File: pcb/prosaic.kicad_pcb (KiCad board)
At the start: 2 copper layers, 347.9 x 95.4 mm, 162 parts, among them J1 USB_C_Receptacle, K1 ESC, K10 WIN, K11 2, K12 W, K13 S, K14 X, K15 LALT, K16 3, K17 E, K18 D, K19 C, K2 TAB, K20 SPACE, K21 4, K22 R, K23 F, K24 V, K25 RALT, K26 5, K27 T, K28 G, K29 B, K3 CAPSLK, K30 FN, K31 6, K32 Y, K33 H, K34 N, K35 MENU, K36 7, K37 U, K38 J, K39 M, K4 LSHIFT, K40 RCTRL, K41 8, K42 I, K43 K, K44 ,, K45 LEFT, K46 9, K47 O, K48 L, K49 ., K5 LCTRL, K50 DOWN, K51 0, K52 P, K53 ;, K54 /, K55 RIGHT, K56 -, K57 [, K58 ', K59 RSHIFT, K6 1, K60 =, K61 ], K62 ENTER, K63 UP, K64 BCKSPC, K65 \, K66 HOME, K67 END, K68 INS, K69 DEL, K7 Q, K70 PGUP, K71 PGDWN, K8 A, K9 Z, SW1 SW_PUSH, U1 ATMEGA32U4, X1 XTAL_GND

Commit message: Made moutning hole rearrangements
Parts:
- removed the REF** at (50.3, 118.8)
- removed the REF** at (388.1, 118.8)
- removed the REF** at (281.7, 137.5)
- removed the REF** at (193.0, 109.2)
- added REF**: MountingHole_3.2mm_M3_ISO7380_Pad, MountingHole:MountingHole_3.2mm_M3_ISO7380_Pad, F.Cu at (388.1, 118.1)
- added REF**: MountingHole_3.2mm_M3_ISO7380_Pad, MountingHole:MountingHole_3.2mm_M3_ISO7380_Pad, F.Cu at (278.7, 146.3)
- added REF**: MountingHole_3.2mm_M3_ISO7380_Pad, MountingHole:MountingHole_3.2mm_M3_ISO7380_Pad, F.Cu at (245.4, 89.8)
- added REF**: MountingHole_3.2mm_M3_ISO7380_Pad, MountingHole:MountingHole_3.2mm_M3_ISO7380_Pad, F.Cu at (164.4, 146.3)
- added REF**: MountingHole_3.2mm_M3_ISO7380_Pad, MountingHole:MountingHole_3.2mm_M3_ISO7380_Pad, F.Cu at (131.1, 89.8)
- added REF**: MountingHole_3.2mm_M3_ISO7380_Pad, MountingHole:MountingHole_3.2mm_M3_ISO7380_Pad, F.Cu at (50.3, 118.1)
- turned R3 to 180 degrees
- turned R4 to 180 degrees
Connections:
- D66 pad 1: /row2 -> /row0
- D67 pad 1: /row3 -> /row1
- D70 pad 1: /row2 -> /row0
- D71 pad 1: /row3 -> /row1
- K20 pad 1: /col3 -> /col5
- K25 pad 1: /col4 -> /col9
- K30 pad 1: /col5 -> /col10
- K35 pad 1: /col6 -> /col11
- K40 pad 1: /col7 -> /col12
- K45 pad 1: /col8 -> /col14
- K50 pad 1: /col9 -> /col15
- K55 pad 1: /col10 -> /col16
- K63 pad 1: /col12 -> /col15
- K66 pad 1: /col13 -> /col15
- K67 pad 1: /col13 -> /col15
- K70 pad 1: /col14 -> /col16
- K71 pad 1: /col14 -> /col16
- U1 pad 36: Net-(U1-Pad36) -> /col16
- U1 pad 37: Net-(U1-Pad37) -> /col15
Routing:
- net /col4: track 426.6 -> 0.00 mm, vias 1 -> 0
- net /row3: track 413.5 -> 0.00 mm, vias 4 -> 0
- net /col0: track 405.1 -> 0.00 mm, vias 1 -> 0
- net /row2: track 395.3 -> 0.00 mm, vias 4 -> 0
- net /col1: track 393.5 -> 0.00 mm, vias 4 -> 0
- net /row4: track 373.7 -> 0.00 mm, vias 1 -> 0
- net /row0: track 361.9 -> 0.00 mm, vias 7 -> 0
- net /row1: track 334.1 -> 0.00 mm, vias 3 -> 0
- net /col3: track 323.9 -> 0.00 mm, vias 4 -> 0
- net /col5: track 271.1 -> 0.00 mm, vias 3 -> 0
- net /col6: track 257.3 -> 0.00 mm, vias 1 -> 0
- net /col7: track 240.2 -> 0.00 mm, vias 1 -> 0
- net /col10: track 238.0 -> 0.00 mm
- net /col8: track 224.9 -> 0.00 mm, vias 1 -> 0
- net /col9: track 224.8 -> 0.00 mm, vias 1 -> 0
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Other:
- board size 347.9 x 95.4 mm -> 347.9 x 95.5 mm

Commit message: WIP: Ready for stabilizer verification
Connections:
- K11 pad 1: Net-(K11-Pad1) -> /col2
- K12 pad 1: Net-(K11-Pad1) -> /col2
- K13 pad 1: Net-(K11-Pad1) -> /col2
- K14 pad 1: Net-(K11-Pad1) -> /col2
- K15 pad 1: Net-(K11-Pad1) -> /col2
- U1 pad 10: /row2 -> /col0
- U1 pad 11: /row3 -> /col1
- U1 pad 12: /col2 -> /row2
- U1 pad 18: /col3 -> /col14
- U1 pad 19: /col4 -> /col15
- U1 pad 20: /col5 -> /col16
- U1 pad 21: /col6 -> /row0
- U1 pad 22: /col8 -> /row1
- U1 pad 25: /col7 -> /row4
- U1 pad 26: /col9 -> /row3
- U1 pad 27: /col10 -> /col13
- U1 pad 28: /row4 -> /col12
- U1 pad 29: /col0 -> /col11
- U1 pad 30: /col1 -> /col10
- U1 pad 31: Net-(U1-Pad31) -> /col9
- U1 pad 32: Net-(U1-Pad32) -> /col8
- U1 pad 36: /col16 -> /col7
- U1 pad 37: /col15 -> /col6
- U1 pad 38: /col14 -> /col5
- U1 pad 39: /col13 -> /col4
- U1 pad 40: /col12 -> /col3
- U1 pad 41: /col11 -> /col2
- U1 pad 8: /row0 -> Net-(U1-Pad8)
- U1 pad 9: /row1 -> Net-(U1-Pad9)

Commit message: Completed revision with new PCB layout
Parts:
- K20: footprint keebs:Mx_Alps_625 -> keebs:Mx_Alps_625_reverse
- moved SW1 0.64 mm to (327.8, 120.4)
- moved J1 0.44 mm to (332.9, 74.6)
- moved R1 0.15 mm to (327.8, 114.2)
- moved C4 0.11 mm to (352.7, 123.9)
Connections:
- D55 pad 1: /row4 -> /row3
- K45 pad 1: /col14 -> /col16
- U1 pad 11: /col1 -> /row2
- U1 pad 12: /row2 -> /col13
- U1 pad 27: /col13 -> /col12
- U1 pad 28: /col12 -> /col11
- U1 pad 29: /col11 -> /col2
- U1 pad 30: /col10 -> /col3
- U1 pad 31: /col9 -> /col4
- U1 pad 32: /col8 -> /col5
- U1 pad 36: /col7 -> /col6
- U1 pad 37: /col6 -> /col7
- U1 pad 38: /col5 -> /col8
- U1 pad 39: /col4 -> /col9
- U1 pad 40: /col3 -> /col10
- U1 pad 41: /col2 -> Net-(U1-Pad41)
- U1 pad 9: Net-(U1-Pad9) -> /col1
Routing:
- net /row0: track 0.00 -> 417.9 mm, vias 0 -> 1
- net /col0: track 0.00 -> 408.4 mm, vias 0 -> 2
- net /col2: track 0.00 -> 405.8 mm
- net /col1: track 0.00 -> 396.4 mm, vias 0 -> 2
- net /col3: track 0.00 -> 360.4 mm
- net /row4: track 0.00 -> 359.8 mm
- net /row3: track 0.00 -> 359.6 mm, vias 0 -> 1
- net /row1: track 0.00 -> 357.3 mm, vias 0 -> 1
- net /col4: track 0.00 -> 341.2 mm
- net /col5: track 0.00 -> 321.5 mm
- net /col6: track 0.00 -> 302.8 mm
- net /row2: track 0.00 -> 292.2 mm, vias 0 -> 1
- net /col7: track 0.00 -> 282.9 mm
- net /col8: track 0.00 -> 260.0 mm
- net /col9: track 0.00 -> 236.8 mm
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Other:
- board text added: "Prosaic Rev A by SiriusSam"
- board text removed: "Prosaic Rev - by SiriusSam"

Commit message: Made trace change around crystal; updated case cad
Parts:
- added R5: 5.1k, Resistor_SMD:R_0805_2012Metric_Pad1.15x1.40mm_HandSolder, B.Cu at (336.0, 83.3)
- added R6: 5.1k, Resistor_SMD:R_0805_2012Metric_Pad1.15x1.40mm_HandSolder, B.Cu at (328.9, 83.3)
- J1: value USB_C_Receptacle -> USB_C_Receptacle_USB2.0; footprint Connector_USB:USB_C_Receptacle_Amphenol_12401610E4-2A -> Connector_USB:USB_C_Receptacle_GCT_USB4085; moved to F.Cu
- moved R4 5.59 mm to (340.6, 109.7), turned to 0 degrees
- moved R3 5.57 mm to (335.2, 109.7), turned to 0 degrees
- moved J1 3.59 mm to (336.0, 76.4), turned to 180 degrees
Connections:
- R3 pad 1: Net-(R3-Pad1) -> Net-(J1-PadA7)
- R3 pad 2: Net-(J1-PadA7) -> Net-(R3-Pad2)
- R4 pad 1: Net-(R4-Pad1) -> Net-(J1-PadA6)
- R4 pad 2: Net-(J1-PadA6) -> Net-(R4-Pad2)
- U1 pad 3: Net-(R3-Pad1) -> Net-(R3-Pad2)
- U1 pad 4: Net-(R4-Pad1) -> Net-(R4-Pad2)
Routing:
- net Net-(R3-Pad2): track 0.00 -> 35.1 mm, vias 0 -> 2
- net Net-(R4-Pad2): track 0.00 -> 22.5 mm, vias 0 -> 2
- net Net-(R3-Pad1): track 21.8 -> 0.00 mm, vias 2 -> 0
- net Net-(R4-Pad1): track 21.4 -> 0.00 mm, vias 2 -> 0
- net Net-(J1-PadB5): track 0.00 -> 13.0 mm
- net Net-(J1-PadA5): track 0.00 -> 6.49 mm
- net Net-(J1-PadA7): track 40.1 -> 35.6 mm, vias 2 -> 0
- net Net-(J1-PadA6): track 34.0 -> 37.5 mm
- net VCC: track 111.0 -> 114.1 mm
- net GND: track 30.2 -> 27.3 mm
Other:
- board text added: "Prosaic Rev A.1 by SiriusSam"
- board text removed: "Prosaic Rev A by SiriusSam"

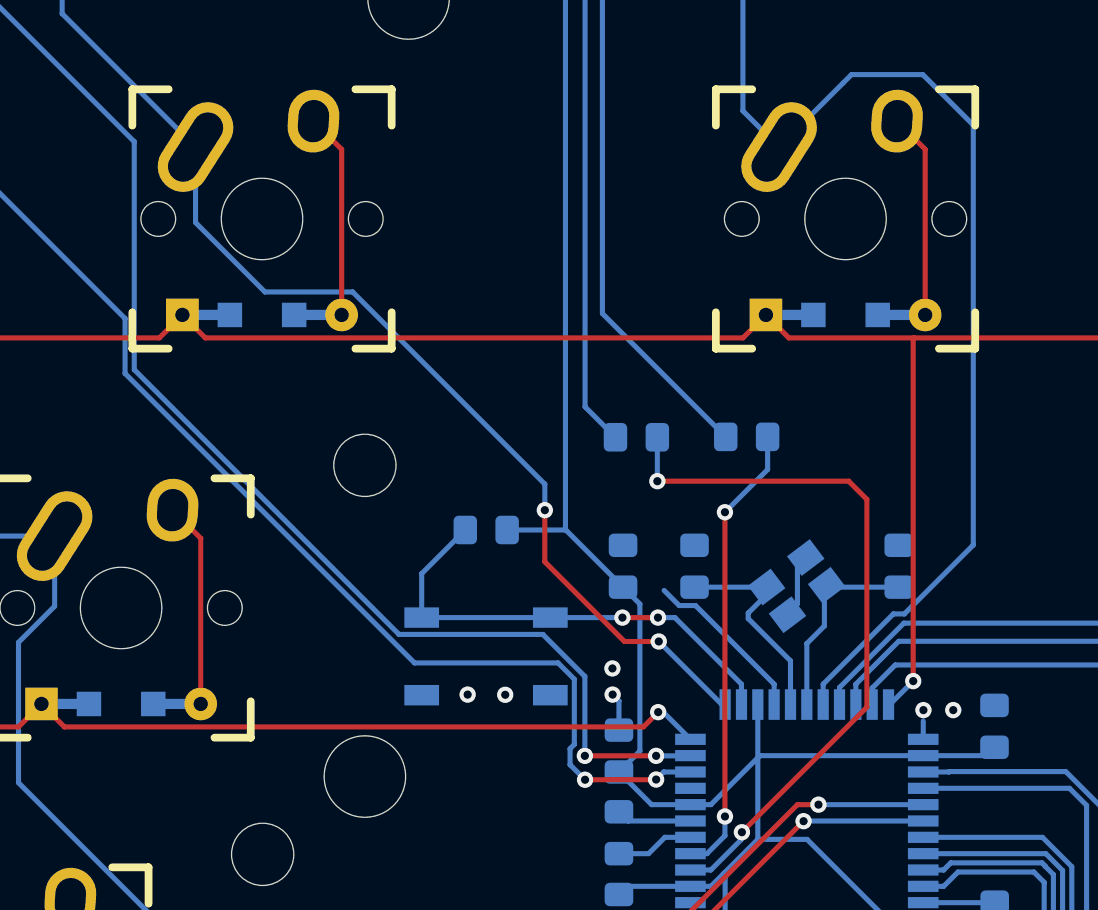
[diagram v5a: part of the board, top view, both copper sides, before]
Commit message: Rerouted VCC trace
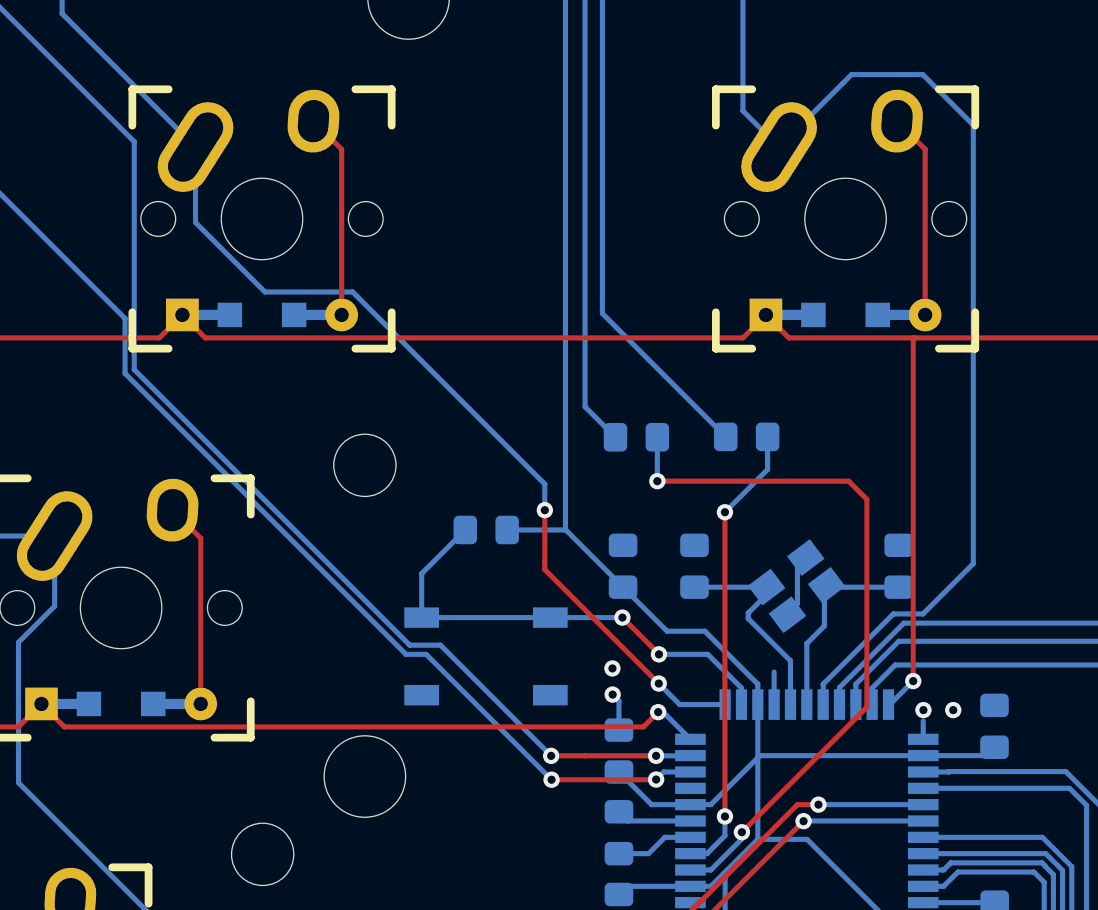
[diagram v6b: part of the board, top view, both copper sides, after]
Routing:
- net GND: track 27.3 -> 20.6 mm, vias 9 -> 7
- net /col1: track 396.4 -> 393.6 mm
- net /col0: track 408.4 -> 406.1 mm
- net /col14: track 64.3 -> 64.8 mm
